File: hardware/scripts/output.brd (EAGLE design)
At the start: 100 x 80 mm, 0 parts

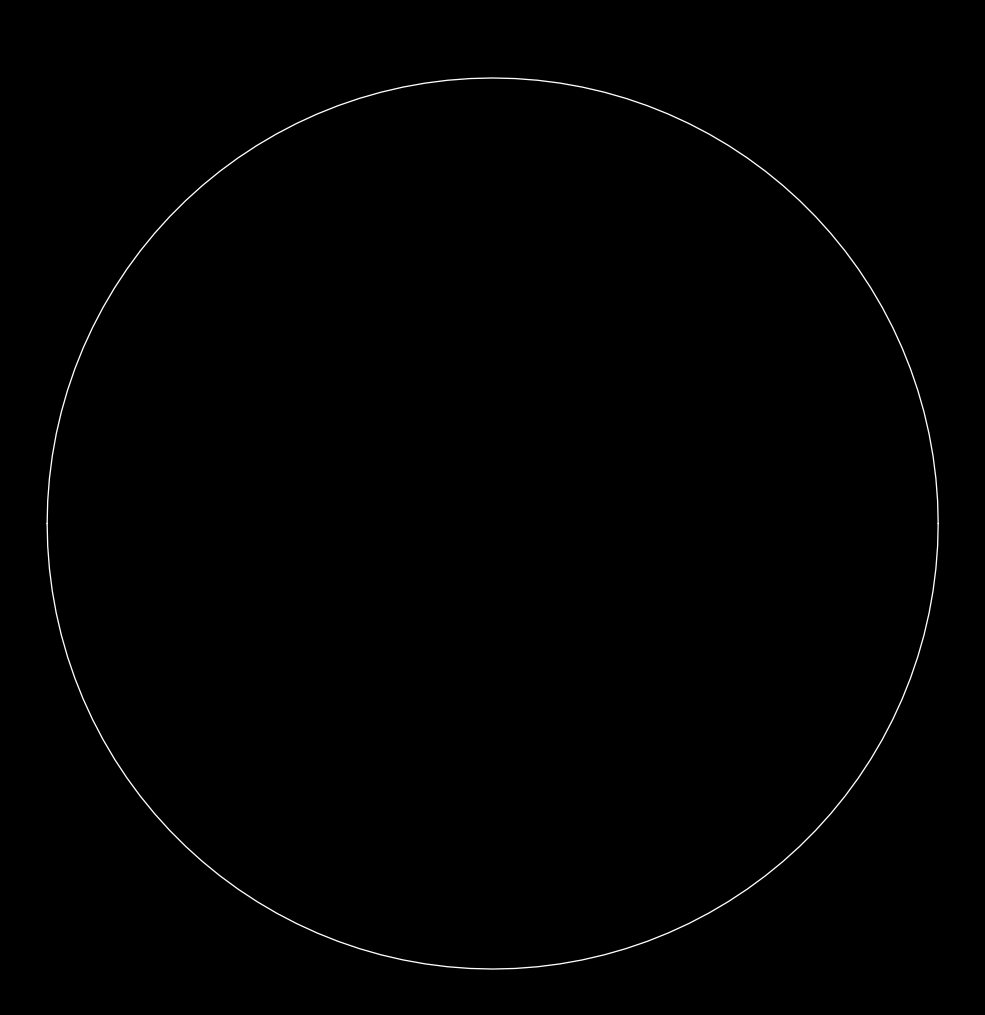
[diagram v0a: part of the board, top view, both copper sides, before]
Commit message: Huge update: added elements, added front-side signals.
Removed offset variables in favor of variables representing the center
of the figure.
User variables written as inches multiplied by 25.4.
Added variables for element ring locations, both for LEDs and headers.
Removed commented code that has already been re-implemented in a
superior way.
Added some comments describing sections of the document.
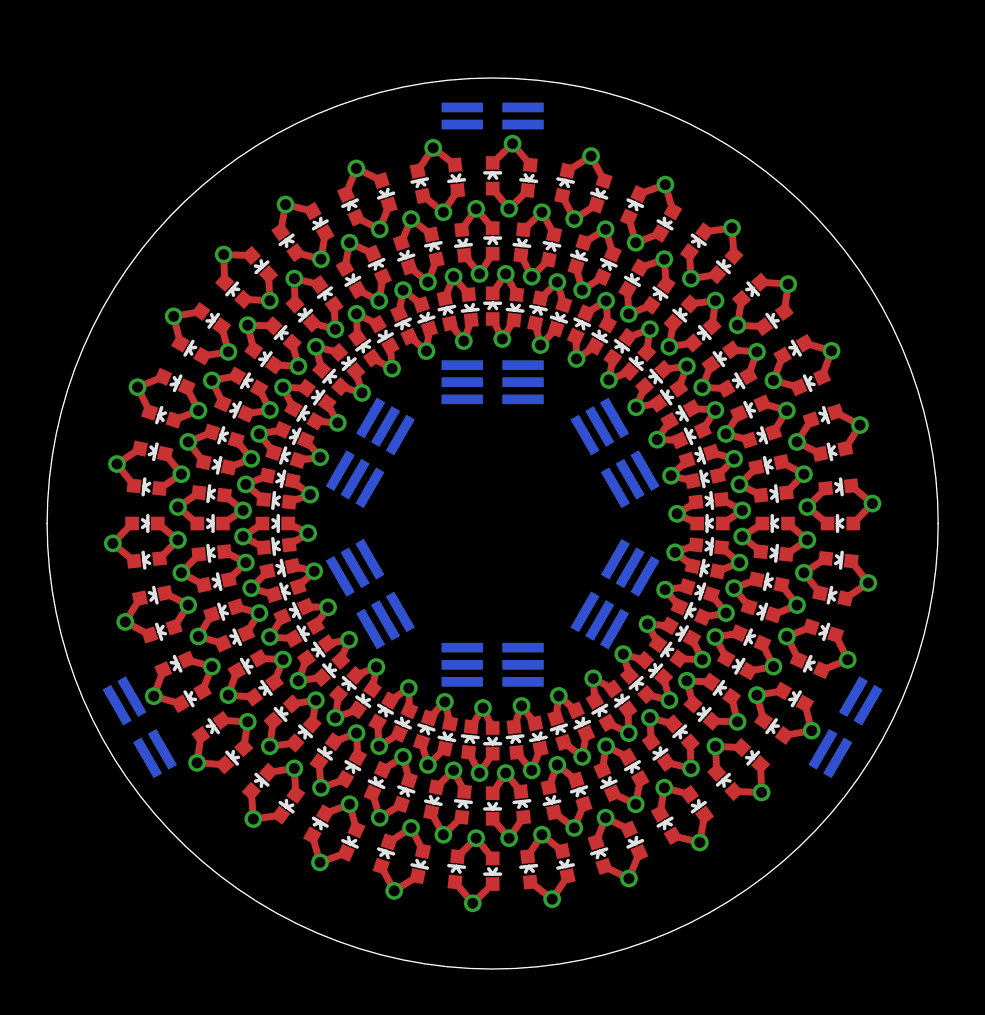
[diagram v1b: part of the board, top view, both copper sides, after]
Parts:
- added H1, H2, H3, H4, H5, H6: 2X3, Customs:3X2_1MM_SMD
- added H7, H8, H9: 2X2, Customs:2X2_1MM_SMD
- added LED1, LED10, LED11, LED12, LED13, LED14, LED15, LED16, LED17, LED18, LED19, LED2, LED20, LED21, LED22, LED23, LED24, LED25, LED26, LED27, LED28, LED29, LED3, LED30, LED31, LED32, LED33, LED34, LED35, LED36, LED37, LED38, LED39, LED4, LED40, LED41, LED42, LED43, LED44, LED45, LED46, LED47, LED48, LED49, LED5, LED50, LED51, LED52, LED53, LED54, LED55, LED56, LED57, LED58, LED59, LED6, LED60, LED7, LED8, LED9: RED, Customs:LED-0603
- added LED100, LED101, LED102, LED103, LED104, LED105, LED106, LED107, LED108, LED109, LED110, LED111, LED112, LED113, LED114, LED115, LED116, LED117, LED118, LED119, LED120, LED61, LED62, LED63, LED64, LED65, LED66, LED67, LED68, LED69, LED70, LED71, LED72, LED73, LED74, LED75, LED76, LED77, LED78, LED79, LED80, LED81, LED82, LED83, LED84, LED85, LED86, LED87, LED88, LED89, LED90, LED91, LED92, LED93, LED94, LED95, LED96, LED97, LED98, LED99: GREEN, Customs:LED-0603
- added LED121, LED122, LED123, LED124, LED125, LED126, LED127, LED128, LED129, LED130, LED131, LED132, LED133, LED134, LED135, LED136, LED137, LED138, LED139, LED140, LED141, LED142, LED143, LED144, LED145, LED146, LED147, LED148, LED149, LED150, LED151, LED152, LED153, LED154, LED155, LED156, LED157, LED158, LED159, LED160, LED161, LED162, LED163, LED164, LED165, LED166, LED167, LED168, LED169, LED170, LED171, LED172, LED173, LED174, LED175, LED176, LED177, LED178, LED179, LED180: BLUE, Customs:LED-0603
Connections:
- new net N$1: LED1.A, LED2.C
- new net N$10: LED19.A, LED20.C
- new net N$100: LED19.C, LED20.A
- new net N$101: LED21.C, LED22.A
- new net N$102: LED23.C, LED24.A
- new net N$103: LED25.C, LED26.A
- new net N$104: LED27.C, LED28.A
- new net N$105: LED29.C, LED30.A
- new net N$106: LED31.C, LED32.A
- new net N$107: LED33.C, LED34.A
- new net N$108: LED35.C, LED36.A
- new net N$109: LED37.C, LED38.A
- new net N$11: LED21.A, LED22.C
- new net N$110: LED39.C, LED40.A
- new net N$111: LED41.C, LED42.A
- new net N$112: LED43.C, LED44.A
- new net N$113: LED45.C, LED46.A
- new net N$114: LED47.C, LED48.A
- new net N$115: LED49.C, LED50.A
- new net N$116: LED51.C, LED52.A
- new net N$117: LED53.C, LED54.A
- new net N$118: LED55.C, LED56.A
- new net N$119: LED57.C, LED58.A
- new net N$12: LED23.A, LED24.C
- new net N$120: LED59.C, LED60.A
- new net N$121: LED62.A, LED63.C
- new net N$122: LED64.A, LED65.C
- new net N$123: LED66.A, LED67.C
- new net N$124: LED68.A, LED69.C
- new net N$125: LED70.A, LED71.C
- new net N$126: LED72.A, LED73.C
- new net N$127: LED74.A, LED75.C
- new net N$128: LED76.A, LED77.C
- new net N$129: LED78.A, LED79.C
- new net N$13: LED25.A, LED26.C
- new net N$130: LED80.A, LED81.C
- new net N$131: LED82.A, LED83.C
- new net N$132: LED84.A, LED85.C
- new net N$133: LED86.A, LED87.C
- new net N$134: LED88.A, LED89.C
- new net N$135: LED90.A, LED91.C
- new net N$136: LED92.A, LED93.C
- new net N$137: LED94.A, LED95.C
- new net N$138: LED96.A, LED97.C
- new net N$139: LED98.A, LED99.C
- new net N$14: LED27.A, LED28.C
- new net N$140: LED100.A, LED101.C
- new net N$141: LED102.A, LED103.C
- new net N$142: LED104.A, LED105.C
- new net N$143: LED106.A, LED107.C
- new net N$144: LED108.A, LED109.C
- new net N$145: LED110.A, LED111.C
- new net N$146: LED112.A, LED113.C
- new net N$147: LED114.A, LED115.C
- new net N$148: LED116.A, LED117.C
- new net N$149: LED118.A, LED119.C
- new net N$15: LED29.A, LED30.C
- new net N$150: LED120.A, LED61.C
- new net N$151: LED121.C, LED122.A
- new net N$152: LED123.C, LED124.A
- new net N$153: LED125.C, LED126.A
- new net N$154: LED127.C, LED128.A
- new net N$155: LED129.C, LED130.A
- new net N$156: LED131.C, LED132.A
- new net N$157: LED133.C, LED134.A
- new net N$158: LED135.C, LED136.A
- new net N$159: LED137.C, LED138.A
- new net N$16: LED31.A, LED32.C
- new net N$160: LED139.C, LED140.A
- new net N$161: LED141.C, LED142.A
- new net N$162: LED143.C, LED144.A
- new net N$163: LED145.C, LED146.A
- new net N$164: LED147.C, LED148.A
- new net N$165: LED149.C, LED150.A
- new net N$166: LED151.C, LED152.A
- new net N$167: LED153.C, LED154.A
- new net N$168: LED155.C, LED156.A
- new net N$169: LED157.C, LED158.A
- new net N$17: LED33.A, LED34.C
- new net N$170: LED159.C, LED160.A
- new net N$171: LED161.C, LED162.A
- new net N$172: LED163.C, LED164.A
- new net N$173: LED165.C, LED166.A
- new net N$174: LED167.C, LED168.A
- new net N$175: LED169.C, LED170.A
- new net N$176: LED171.C, LED172.A
- new net N$177: LED173.C, LED174.A
- new net N$178: LED175.C, LED176.A
- new net N$179: LED177.C, LED178.A
- new net N$18: LED35.A, LED36.C
- new net N$180: LED179.C, LED180.A
- new net N$19: LED37.A, LED38.C
- new net N$2: LED3.A, LED4.C
- new net N$20: LED39.A, LED40.C
- new net N$21: LED41.A, LED42.C
- new net N$22: LED43.A, LED44.C
- new net N$23: LED45.A, LED46.C
- new net N$24: LED47.A, LED48.C
- new net N$25: LED49.A, LED50.C
- new net N$26: LED51.A, LED52.C
- new net N$27: LED53.A, LED54.C
- new net N$28: LED55.A, LED56.C
- new net N$29: LED57.A, LED58.C
- new net N$3: LED5.A, LED6.C
- new net N$30: LED59.A, LED60.C
- new net N$31: LED62.C, LED63.A
- new net N$32: LED64.C, LED65.A
- new net N$33: LED66.C, LED67.A
- new net N$34: LED68.C, LED69.A
- new net N$35: LED70.C, LED71.A
- new net N$36: LED72.C, LED73.A
- new net N$37: LED74.C, LED75.A
- new net N$38: LED76.C, LED77.A
- new net N$39: LED78.C, LED79.A
- new net N$4: LED7.A, LED8.C
- new net N$40: LED80.C, LED81.A
- new net N$41: LED82.C, LED83.A
- new net N$42: LED84.C, LED85.A
- new net N$43: LED86.C, LED87.A
- new net N$44: LED88.C, LED89.A
- new net N$45: LED90.C, LED91.A
- new net N$46: LED92.C, LED93.A
- new net N$47: LED94.C, LED95.A
- new net N$48: LED96.C, LED97.A
- new net N$49: LED98.C, LED99.A
- new net N$5: LED10.C, LED9.A
- new net N$50: LED100.C, LED101.A
- new net N$51: LED102.C, LED103.A
- new net N$52: LED104.C, LED105.A
- new net N$53: LED106.C, LED107.A
- new net N$54: LED108.C, LED109.A
- new net N$55: LED110.C, LED111.A
- new net N$56: LED112.C, LED113.A
- new net N$57: LED114.C, LED115.A
- new net N$58: LED116.C, LED117.A
- new net N$59: LED118.C, LED119.A
- new net N$6: LED11.A, LED12.C
- new net N$60: LED120.C, LED61.A
- new net N$61: LED121.A, LED122.C
- new net N$62: LED123.A, LED124.C
- new net N$63: LED125.A, LED126.C
- new net N$64: LED127.A, LED128.C
- new net N$65: LED129.A, LED130.C
- new net N$66: LED131.A, LED132.C
- new net N$67: LED133.A, LED134.C
- new net N$68: LED135.A, LED136.C
- new net N$69: LED137.A, LED138.C
- new net N$7: LED13.A, LED14.C
- new net N$70: LED139.A, LED140.C
- new net N$71: LED141.A, LED142.C
- new net N$72: LED143.A, LED144.C
- new net N$73: LED145.A, LED146.C
- new net N$74: LED147.A, LED148.C
- new net N$75: LED149.A, LED150.C
- new net N$76: LED151.A, LED152.C
- new net N$77: LED153.A, LED154.C
- new net N$78: LED155.A, LED156.C
- new net N$79: LED157.A, LED158.C
- new net N$8: LED15.A, LED16.C
- new net N$80: LED159.A, LED160.C
- new net N$81: LED161.A, LED162.C
- new net N$82: LED163.A, LED164.C
- new net N$83: LED165.A, LED166.C
- new net N$84: LED167.A, LED168.C
- new net N$85: LED169.A, LED170.C
- new net N$86: LED171.A, LED172.C
- new net N$87: LED173.A, LED174.C
- new net N$88: LED175.A, LED176.C
- new net N$89: LED177.A, LED178.C
- new net N$9: LED17.A, LED18.C
- new net N$90: LED179.A, LED180.C
- new net N$91: LED1.C, LED2.A
- new net N$92: LED3.C, LED4.A
- new net N$93: LED5.C, LED6.A
- new net N$94: LED7.C, LED8.A
- new net N$95: LED10.A, LED9.C
- new net N$96: LED11.C, LED12.A
- new net N$97: LED13.C, LED14.A
- new net N$98: LED15.C, LED16.A
- new net N$99: LED17.C, LED18.A
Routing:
- net N$157: track 0.00 -> 3.24 mm, vias 0 -> 1
- net N$152: track 0.00 -> 3.24 mm, vias 0 -> 1
- net N$172: track 0.00 -> 3.24 mm, vias 0 -> 1
- net N$167: track 0.00 -> 3.24 mm, vias 0 -> 1
- net N$171: track 0.00 -> 3.24 mm, vias 0 -> 1
- net N$168: track 0.00 -> 3.24 mm, vias 0 -> 1
- net N$156: track 0.00 -> 3.24 mm, vias 0 -> 1
- net N$153: track 0.00 -> 3.24 mm, vias 0 -> 1
- net N$170: track 0.00 -> 3.24 mm, vias 0 -> 1
- net N$169: track 0.00 -> 3.24 mm, vias 0 -> 1
- net N$155: track 0.00 -> 3.24 mm, vias 0 -> 1
- net N$154: track 0.00 -> 3.24 mm, vias 0 -> 1
- net N$177: track 0.00 -> 3.24 mm, vias 0 -> 1
- net N$162: track 0.00 -> 3.24 mm, vias 0 -> 1
- net N$179: track 0.00 -> 3.24 mm, vias 0 -> 1
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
